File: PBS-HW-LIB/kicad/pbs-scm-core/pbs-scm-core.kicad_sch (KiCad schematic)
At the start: 0 parts

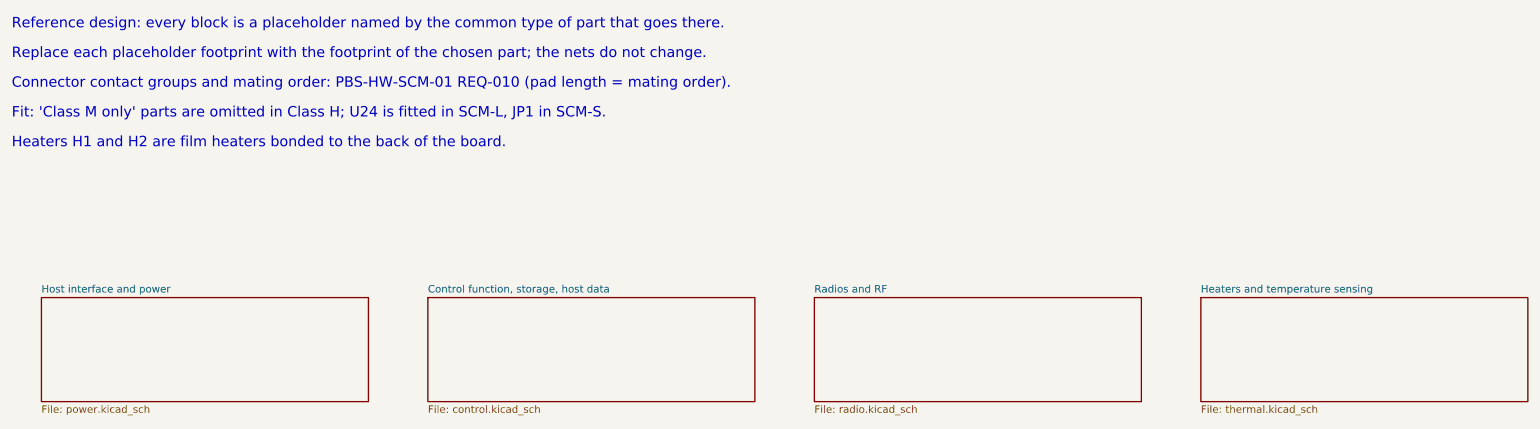
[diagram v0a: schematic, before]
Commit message: Define the module host connector (PBS-HW-CON-01)
Add PBS-HW-CON-01: a face-to-face blind-mate connector with 17 contacts at
stated positions, flat pads on the module and spring contacts in the bay,
mating order set by four free heights 0.60 mm apart, keyed guide pins
(A 4.00, B 3.00), a bay cover plate and covered module apertures, an SMP
RF contact, forces and electrical ratings. Two dimensioned drawing sheets.

KiCad: both J1 footprints now follow the contact map (module half on the
back of the core board, centred; bay half with spring-contact holes and
guide pins), with 3D models showing contact heights, guide pins and the
cover plate. All geometry comes from tools/connector.py.

PBS-HW-SCM-01 v0.3 references the connector document.
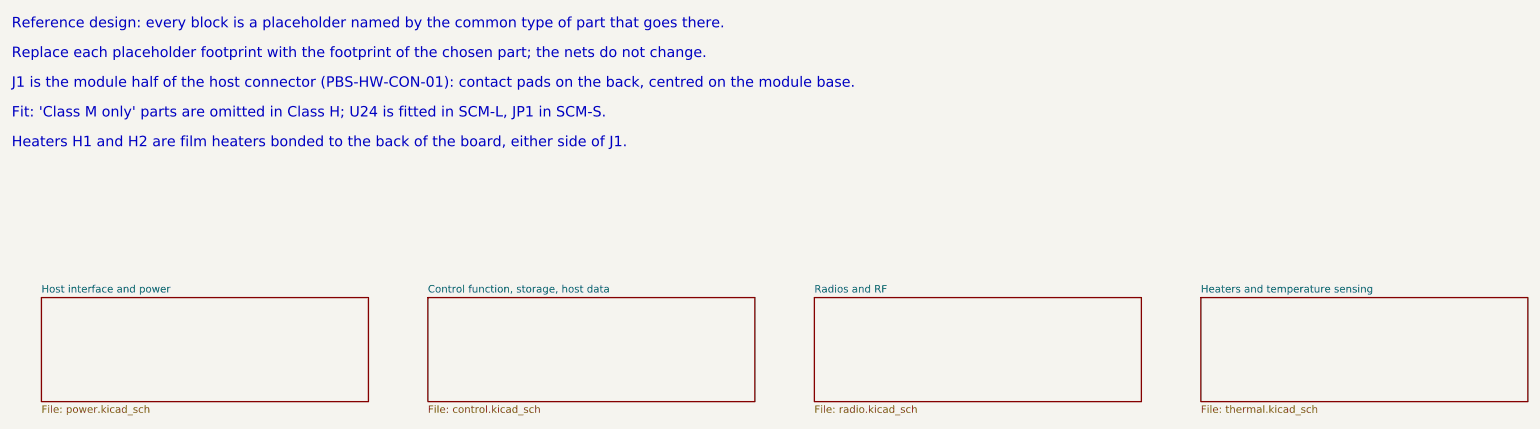
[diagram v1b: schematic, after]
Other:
- note added: "Heaters H1 and H2 are film heaters bonded to the back of the board, either side of J1."
- note added: "J1 is the module half of the host connector (PBS-HW-CON-01): contact pads on the back, centred on the module base."
- note removed: "Connector contact groups and mating order: PBS-HW-SCM-01 REQ-010 (pad length = mating order)."
- note removed: "Heaters H1 and H2 are film heaters bonded to the back of the board."
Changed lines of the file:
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@@
 (kicad_sch (version 20231120) (generator "eeschema") (generator_version "8.0")
   (paper "A4")
-  (title_block (title "PBS-HW-SCM-01 Surface Communication Module, core board") (date "2026-10-08") (rev "0.2") (company "Pale Blue Systems Foundation") (comment 1 "PBS-HW-SCM-01 open reference design; generic placeholders, no part numbers") (comment 2 "Generated by PBS-HW-LIB/kicad/tools/generate.py"))
+  (title_block (title "PBS-HW-SCM-01 Surface Communication Module, core board") (date "2026-10-08") (rev "0.3") (company "Pale Blue Systems Foundation") (comment 1 "PBS-HW-SCM-01 open reference design; generic placeholders, no part numbers") (comment 2 "Generated by PBS-HW-LIB/kicad/tools/generate.py"))
   (text "Reference design: every block is a placeholder named by the common type of part that goes there." (exclude_from_sim no) (at 20.32 30.48 0) (effects (font (size 1.778 1.778)) (justify left bottom)))
   (text "Replace each placeholder footprint with the footprint of the chosen part; the nets do not change." (exclude_from_sim no) (at 20.32 35.56 0) (effects (font (size 1.778 1.778)) (justify left bottom)))
-  (text "Connector contact groups and mating order: PBS-HW-SCM-01 REQ-010 (pad length = mating order)." (exclude_from_sim no) (at 20.32 40.64 0) (effects (font (size 1.778 1.778)) (justify left bottom)))
+  (text "J1 is the module half of the host connector (PBS-HW-CON-01): contact pads on the back, centred on the module base." (exclude_from_sim no) (at 20.32 40.64 0) (effects (font (size 1.778 1.778)) (justify left bottom)))
   (text "Fit: 'Class M only' parts are omitted in Class H; U24 is fitted in SCM-L, JP1 in SCM-S." (exclude_from_sim no) (at 20.32 45.72 0) (effects (font (size 1.778 1.778)) (justify left bottom)))
-  (text "Heaters H1 and H2 are film heaters bonded to the back of the board." (exclude_from_sim no) (at 20.32 50.8 0) (effects (font (size 1.778 1.778)) (justify left bottom)))
+  (text "Heaters H1 and H2 are film heaters bonded to the back of the board, either side of J1." (exclude_from_sim no) (at 20.32 50.8 0) (effects (font (size 1.778 1.778)) (justify left bottom)))
   (sheet (at 25.4 76.2) (size 55.88 17.78) (exclude_from_sim no) (in_bom yes) (on_board yes) (dnp no) (fields_autoplaced yes) (stroke (width 0.1524) (type solid)) (fill (color 0 0 0 0.0000)) (property "Sheetname" "Host interface and power" (at 25.4 75.4884 0) (effects (font (size 1.27 1.27)) (justify left bottom))) (property "Sheetfile" "power.kicad_sch" (at 25.4 94.5716 0) (effects (font (size 1.27 1.27)) (justify left top))) (instances (project "pbs-scm-core" (path "/0b84a1f5-035b-569f-a092-a30049d82087" (page "2")))))
   (sheet (at 91.44 76.2) (size 55.88 17.78) (exclude_from_sim no) (in_bom yes) (on_board yes) (dnp no) (fields_autoplaced yes) (stroke (width 0.1524) (type solid)) (fill (color 0 0 0 0.0000)) (property "Sheetname" "Control function, storage, host data" (at 91.44 75.4884 0) (effects (font (size 1.27 1.27)) (justify left bottom))) (property "Sheetfile" "control.kicad_sch" (at 91.44 94.5716 0) (effects (font (size 1.27 1.27)) (justify left top))) (instances (project "pbs-scm-core" (path "/0b84a1f5-035b-569f-a092-a30049d82087" (page "3")))))
